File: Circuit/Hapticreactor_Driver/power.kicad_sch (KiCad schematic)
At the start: 7 parts, among them IC1 XCL103D503CR-G, J3 Conn_01x02

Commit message: ハプティックリアクタ用基板完成
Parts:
- removed C3, C4: 10u, Capacitor_SMD:C_1206_3216Metric_Pad1.33x1.80mm_HandSolder, symbol Device:C
- removed IC1: XCL103D503CR-G, XCL103D503CRG, symbol XCL103D503CR-G:XCL103D503CR-G
- removed R7: 10k, Resistor_SMD:R_0603_1608Metric_Pad0.98x0.95mm_HandSolder, symbol Device:R

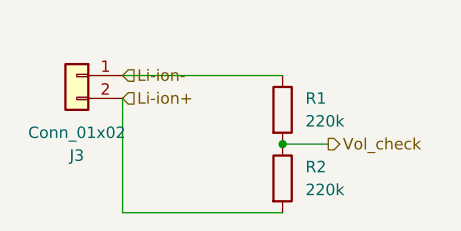
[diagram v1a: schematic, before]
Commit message: VMをバッテリ入力に変更，バッテリ周りの間違いを訂正
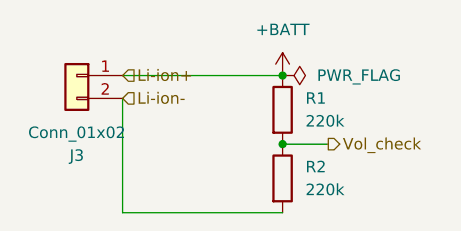
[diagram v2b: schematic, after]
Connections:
- net Li-ion+ is gone; now on net Li-ion-: J3.2 (Pin_2), R2.2
- net Li-ion-: no longer J3.1 (Pin_1), R1.1
- new net +BATT: J3.1 (Pin_1), R1.1
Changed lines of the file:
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@@
 	(paper "A4")
+	(junction
+		(at 90.17 43.18)
+		(diameter 0)
+		(color 0 0 0 0)
+	)
 	(junction
 		(at 90.17 50.8)
@@
 	(hierarchical_label "Li-ion+"
 		(shape input)
-		(at 72.39 45.72 0)
+		(at 72.39 43.18 0)
 		(effects
 			(font
@@
 	(hierarchical_label "Li-ion-"
 		(shape input)
-		(at 72.39 43.18 0)
+		(at 72.39 45.72 0)
 		(effects
 			(font
@@
 			)
 			(justify left)
+		)
+	)
+	(symbol
+		(lib_id "power:+BATT")
+		(at 90.17 43.18 0)
+		(unit 1)
+		(exclude_from_sim no)
+		(in_bom yes)
+		(on_board yes)
+		(dnp no)
+		(fields_autoplaced yes)
+		(property "Reference" "#PWR014"
+			(at 90.17 46.99 0)
+			(effects
+				(font
+					(size 1.27 1.27)
+				)
+				(hide yes)
+			)
+		)
+		(property "Value" "+BATT"
+			(at 90.17 38.1 0)
+			(effects
+				(font
+					(size 1.27 1.27)
+				)
+			)
+		)
+		(property "Footprint" ""
+			(at 90.17 43.18 0)
+			(effects
+				(font
+					(size 1.27 1.27)
+				)
+				(hide yes)
+			)
+		)
+		(property "Datasheet" ""
+			(at 90.17 43.18 0)
+			(effects
+				(font
+					(size 1.27 1.27)
+				)
+				(hide yes)
+			)
+		)
+		(property "Description" "Power symbol creates a global label with name \"+BATT\""
+			(at 90.17 43.18 0)
+			(effects
+				(font
+					(size 1.27 1.27)
+				)
+				(hide yes)
+			)
+		)
+		(pin "1"
+		)
+		(instances
+			(project ""
+				(path "/2de60640-83cc-436b-97a4-426b15b610d6/ab66820f-d4de-445a-808f-ae0431d3c659"
+					(reference "#PWR014")
+					(unit 1)
+				)
+			)
 		)
 	)
@@
 					(unit 1)
 				)
+			)
+		)
+	)
+	(symbol
+		(lib_id "power:PWR_FLAG")
+		(at 90.17 43.18 270)
+		(unit 1)
+		(exclude_from_sim no)
+		(in_bom yes)
+		(on_board yes)
+		(dnp no)
+		(fields_autoplaced yes)
+		(property "Reference" "#FLG02"
+			(at 92.075 43.18 0)
+			(effects
+				(font
+					(size 1.27 1.27)
+				)
+				(hide yes)
+			)
+		)
+		(property "Value" "PWR_FLAG"
+			(at 93.98 43.1799 90)
+			(effects
+				(font
+					(size 1.27 1.27)
+				)
+				(justify left)
+			)
+		)
+		(property "Footprint" ""
+			(at 90.17 43.18 0)
+			(effects
+				(font
+					(size 1.27 1.27)
+				)
+				(hide yes)
+			)
+		)
+		(property "Datasheet" "~"
+			(at 90.17 43.18 0)
+			(effects
+				(font
+					(size 1.27 1.27)
+				)
+				(hide yes)
+			)
+		)
+		(property "Description" "Special symbol for telling ERC where power comes from"
+			(at 90.17 43.18 0)
+			(effects
+				(font
+					(size 1.27 1.27)
+				)
+				(hide yes)
+			)
+		)
+		(pin "1"
+		)
+		(instances
+			(project ""
+				(path "/2de60640-83cc-436b-97a4-426b15b610d6/ab66820f-d4de-445a-808f-ae0431d3c659"
+					(reference "#FLG02")
+					(unit 1)
+				)

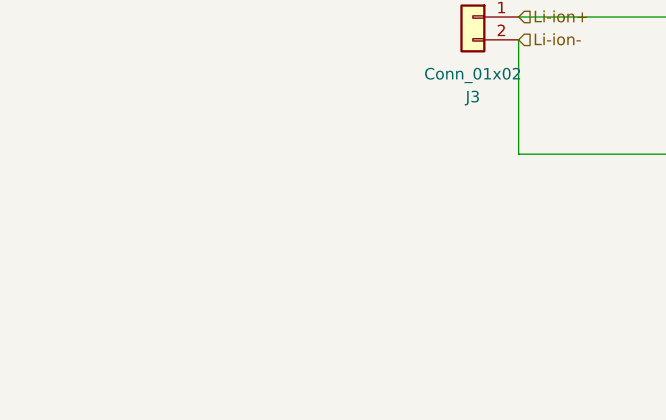
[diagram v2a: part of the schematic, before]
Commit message: 秋野の回路に昇圧DCDCつけて東芝MDつけた
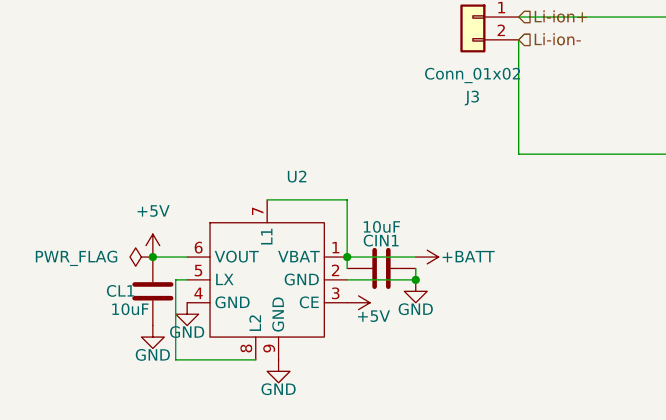
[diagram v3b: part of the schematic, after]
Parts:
- added CIN1, CL1: 10uF, Capacitor_SMD:C_0603_1608Metric, symbol Device:C
- added U2: ~, 0_MyFootprintLibrary:XCL102D503CR-G, symbol 0_MySymbolLibrary:XCL102D503CR-G
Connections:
- net +BATT: now also CIN1.1, U2.1 (VBAT), U2.7 (L1)
- new net: U2.5 (LX), U2.8 (L2)
- new net +5V: CL1.2, U2.3 (CE), U2.6 (VOUT)
- new net GND: CIN1.2, CL1.1, U2.2 (GND), U2.4 (GND), U2.9 (GND)

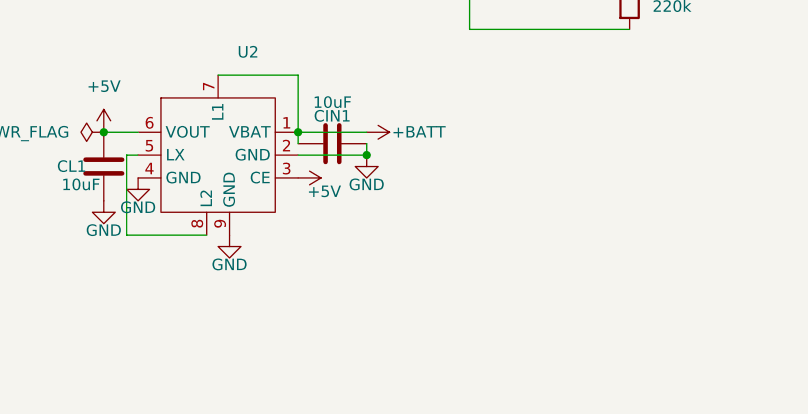
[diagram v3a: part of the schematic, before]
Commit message: スイッチを追加した．とりあえずこれで一旦発注しました
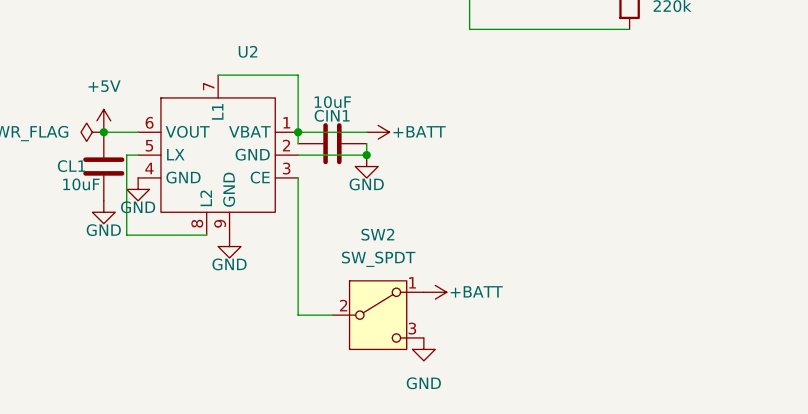
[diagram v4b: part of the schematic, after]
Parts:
- added SW2: SW_SPDT, 0_MyFootprintLibrary:SSAJ120100, symbol Switch:SW_SPDT
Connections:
- net +5V: no longer U2.3 (CE)
- net +BATT: now also SW2.1 (A)
- net GND: now also SW2.3 (C)
- new net: SW2.2 (B), U2.3 (CE)
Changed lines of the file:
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@@
+	(wire
+		(pts
+			(xy 53.34 90.17) (xy 57.15 90.17)
+		)
+		(stroke
+			(width 0)
+			(type default)
+		)
+	)
 	(wire
 		(pts
@@
 		(pts
 			(xy 72.39 45.72) (xy 72.39 58.42)
+		)
+		(stroke
+			(width 0)
+			(type default)
+		)
+	)
+	(wire
+		(pts
+			(xy 53.34 74.93) (xy 53.34 90.17)
 		)
 		(stroke
@@
 	)
 	(symbol
+		(lib_id "Switch:SW_SPDT")
+		(at 62.23 90.17 0)
+		(unit 1)
+		(exclude_from_sim no)
+		(in_bom yes)
+		(on_board yes)
+		(dnp no)
+		(fields_autoplaced yes)
+		(property "Reference" "SW2"
+			(at 62.23 81.28 0)
+			(effects
+				(font
+					(size 1.27 1.27)
+				)
+			)
+		)
+		(property "Value" "SW_SPDT"
+			(at 62.23 83.82 0)
+			(effects
+				(font
+					(size 1.27 1.27)
+				)
+			)
+		)
+		(property "Footprint" "0_MyFootprintLibrary:SSAJ120100"
+			(at 62.23 90.17 0)
+			(effects
+				(font
+					(size 1.27 1.27)
+				)
+				(hide yes)
+			)
+		)
+		(property "Datasheet" "~"
+			(at 62.23 97.79 0)
+			(effects
+				(font
+					(size 1.27 1.27)
+				)
+				(hide yes)
+			)
+		)
+		(property "Description" "Switch, single pole double throw"
+			(at 62.23 90.17 0)
+			(effects
+				(font
+					(size 1.27 1.27)
+				)
+				(hide yes)
+			)
+		)
+		(pin "2"
+		)
+		(pin "1"
+		)
+		(pin "3"
+		)
+		(instances
+			(project ""
+				(path "/2de60640-83cc-436b-97a4-426b15b610d6/ab66820f-d4de-445a-808f-ae0431d3c659"
+					(reference "SW2")
+					(unit 1)
+				)
+			)
+		)
+	)
+	(symbol
 		(lib_id "power:GND")
 		(at 45.72 81.28 0)
@@
 				(path "/2de60640-83cc-436b-97a4-426b15b610d6/ab66820f-d4de-445a-808f-ae0431d3c659"
 					(reference "#PWR016")
+					(unit 1)
+				)
+			)
+		)
+	)
+	(symbol
+		(lib_id "power:+BATT")
+		(at 67.31 87.63 270)
+		(unit 1)
+		(exclude_from_sim no)
+		(in_bom yes)
+		(on_board yes)
+		(dnp no)
+		(property "Reference" "#PWR017"
+			(at 63.5 87.63 0)
+			(effects
+				(font
+					(size 1.27 1.27)
+				)
+				(hide yes)
+			)
+		)
+		(property "Value" "+BATT"
+			(at 70.104 87.63 90)
+			(effects
+				(font
+					(size 1.27 1.27)
+				)
+				(justify left)
+			)
+		)
+		(property "Footprint" ""
+			(at 67.31 87.63 0)
+			(effects
+				(font
+					(size 1.27 1.27)
+				)
+				(hide yes)
+			)
+		)
+		(property "Datasheet" ""
+			(at 67.31 87.63 0)
+			(effects
+				(font
+					(size 1.27 1.27)
+				)
+				(hide yes)
+			)
+		)
+		(property "Description" "Power symbol creates a global label with name \"+BATT\""
+			(at 67.31 87.63 0)
+			(effects
+				(font
+					(size 1.27 1.27)
+				)
+				(hide yes)
+			)
+		)
+		(pin "1"
+		)
+		(instances
+			(project "Hapticreactor_Driver"
+				(path "/2de60640-83cc-436b-97a4-426b15b610d6/ab66820f-d4de-445a-808f-ae0431d3c659"
+					(reference "#PWR017")
 					(unit 1)
 				)
@@
 	)
 	(symbol
+		(lib_id "power:GND")
+		(at 67.31 92.71 0)
+		(unit 1)
+		(exclude_from_sim no)
+		(in_bom yes)
+		(on_board yes)
+		(dnp no)
+		(fields_autoplaced yes)
+		(property "Reference" "#PWR025"
+			(at 67.31 99.06 0)
+			(effects
+				(font
+					(size 1.27 1.27)
+				)
+				(hide yes)
+			)
+		)
+		(property "Value" "GND"
+			(at 67.31 97.79 0)
+			(effects
+				(font
+					(size 1.27 1.27)
+				)
+			)
+		)
+		(property "Footprint" ""
+			(at 67.31 92.71 0)
+			(effects
+				(font
+					(size 1.27 1.27)
+				)
+				(hide yes)
+			)
+		)
+		(property "Datasheet" ""
+			(at 67.31 92.71 0)
+			(effects
+				(font
+					(size 1.27 1.27)
+				)
+				(hide yes)
+			)
+		)
+		(property "Description" "Power symbol creates a global label with name \"GND\" , ground"
+			(at 67.31 92.71 0)
+			(effects
+				(font
+					(size 1.27 1.27)
+				)
+				(hide yes)
+			)
+		)
+		(pin "1"
+		)
+		(instances
+			(project ""
+				(path "/2de60640-83cc-436b-97a4-426b15b610d6/ab66820f-d4de-445a-808f-ae0431d3c659"
+					(reference "#PWR025")
+					(unit 1)
+				)
+			)
+		)
+	)
+	(symbol
 		(lib_id "0_MySymbolLibrary:XCL102D503CR-G")
 		(at 44.45 53.34 0)
@@
 					(unit 1)
 				)
-			)
-		)
-	)
-	(symbol
-		(lib_id "power:+5V")
-		(at 53.34 74.93 270)
-		(unit 1)
-		(exclude_from_sim no)
-		(in_bom yes)
-		(on_board yes)
-		(dnp no)
-		(property "Reference" "#PWR017"
-			(at 49.53 74.93 0)
-			(effects
-				(font
-					(size 1.27 1.27)
-				)
-				(hide yes)
-			)
-		)
-		(property "Value" "+5V"
-			(at 54.356 76.454 90)
-			(effects
-				(font
-					(size 1.27 1.27)
-				)
-				(justify left)
-			)
-		)
-		(property "Footprint" ""
-			(at 53.34 74.93 0)
-			(effects
-				(font
-					(size 1.27 1.27)
-				)
-				(hide yes)
-			)
-		)
-		(property "Datasheet" ""
-			(at 53.34 74.93 0)
-			(effects
-				(font
-					(size 1.27 1.27)
-				)
-				(hide yes)
-			)
-		)
-		(property "Description" "Power symbol creates a global label with name \"+5V\""
-			(at 53.34 74.93 0)
-			(effects
-				(font
-					(size 1.27 1.27)
-				)
-				(hide yes)
-			)
-		)
-		(pin "1"
-		)
-		(instances
-			(project "Hapticreactor_Driver"
-				(path "/2de60640-83cc-436b-97a4-426b15b610d6/ab66820f-d4de-445a-808f-ae0431d3c659"
-					(reference "#PWR017")
-					(unit 1)
-				)
